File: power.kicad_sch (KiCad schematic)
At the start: 40 parts, among them J2 BATT_CON, J3 PWR_HDR, U2 BQ25622, U6 MIC2876-5.25YMT-TR

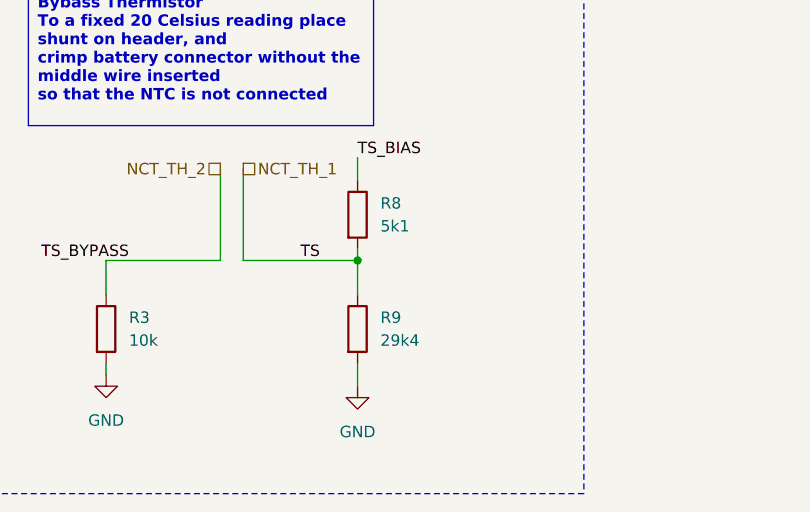
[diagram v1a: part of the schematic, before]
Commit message: fix: NTC resistor values
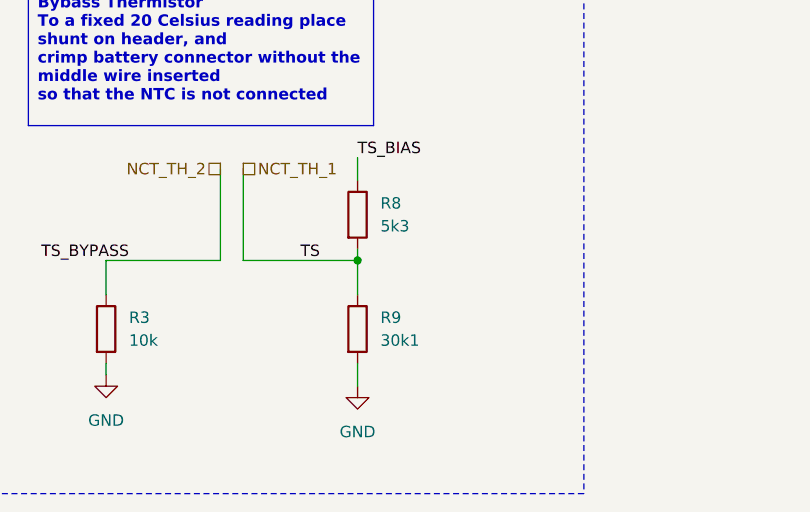
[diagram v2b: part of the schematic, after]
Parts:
- R8: value 5k1 -> 5k3; MPN ERA-2AEB512X -> RT0402DRE075K3L
- R9: value 29k4 -> 30k1; MPN ERJ-2RKF2942X -> ERA-2AEB3012X
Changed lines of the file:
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@@
 			)
 		)
-		(property "Value" "29k4"
+		(property "Value" "30k1"
 			(at 135.89 179.07 0)
 			(effects
@@
 			)
 		)
-		(property "MPN" "ERJ-2RKF2942X"
+		(property "MPN" "ERA-2AEB3012X"
 			(at 133.35 177.8 0)
 			(effects
@@
 			)
 		)
-		(property "Value" "5k1"
+		(property "Value" "5k3"
 			(at 135.89 166.37 0)
 			(effects
@@
 			)
 		)
-		(property "MPN" "ERA-2AEB512X"
+		(property "MPN" "RT0402DRE075K3L"
 			(at 133.35 165.1 0)
 			(effects

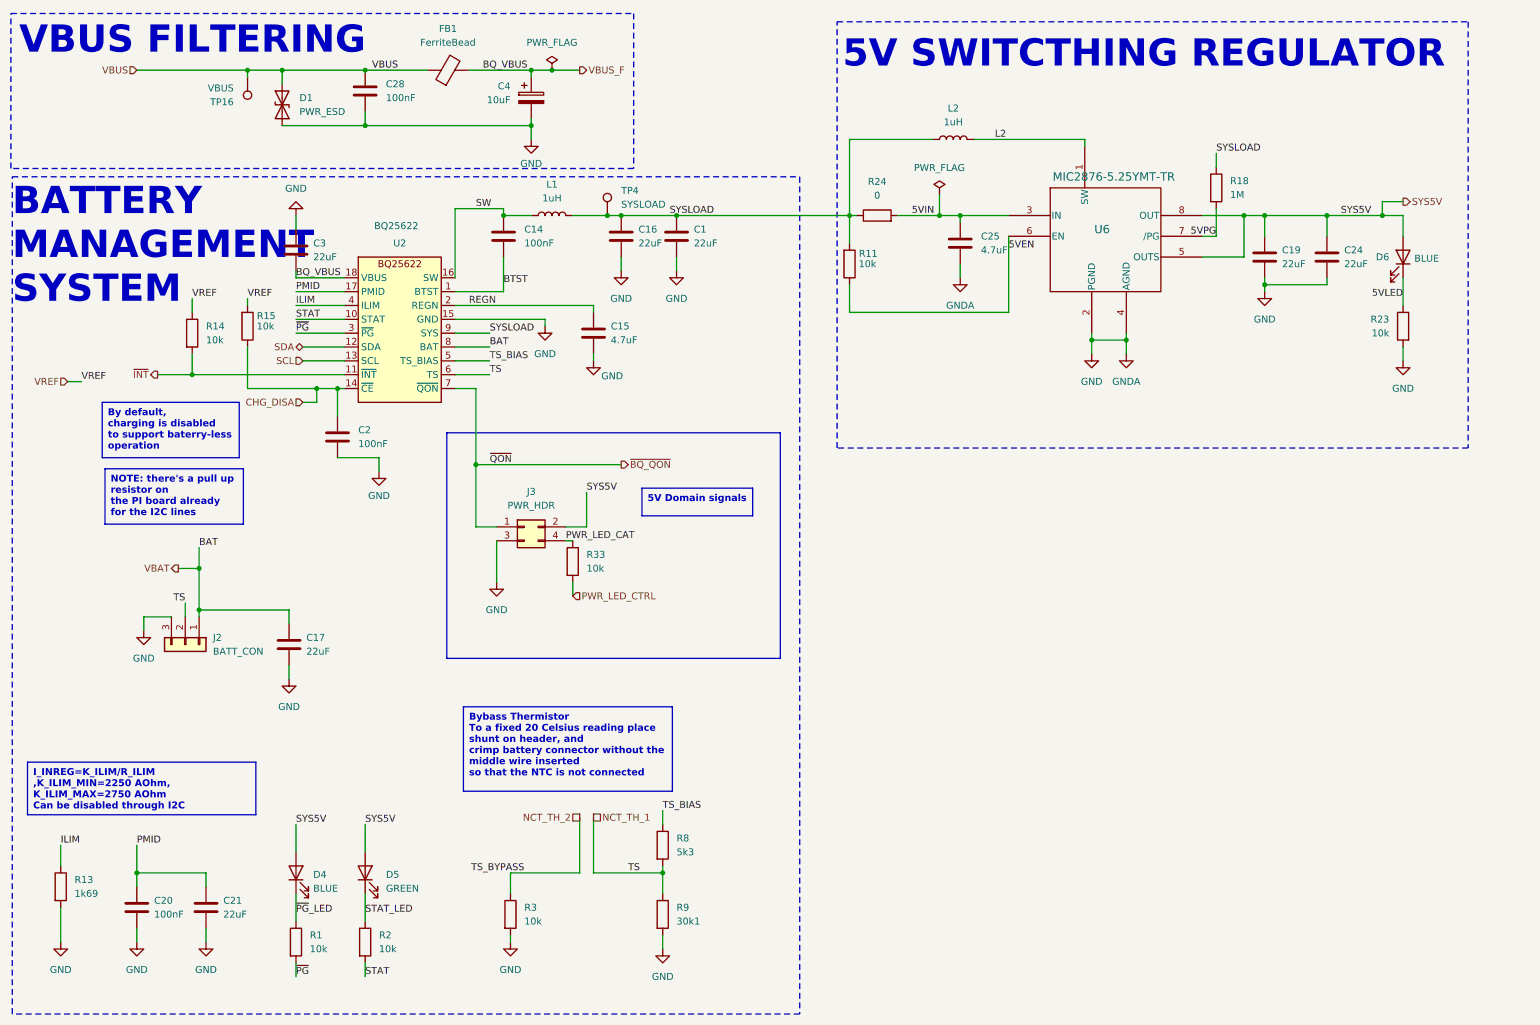
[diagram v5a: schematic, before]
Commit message: feat: 3V3 regulator + complete rework to 16 layers
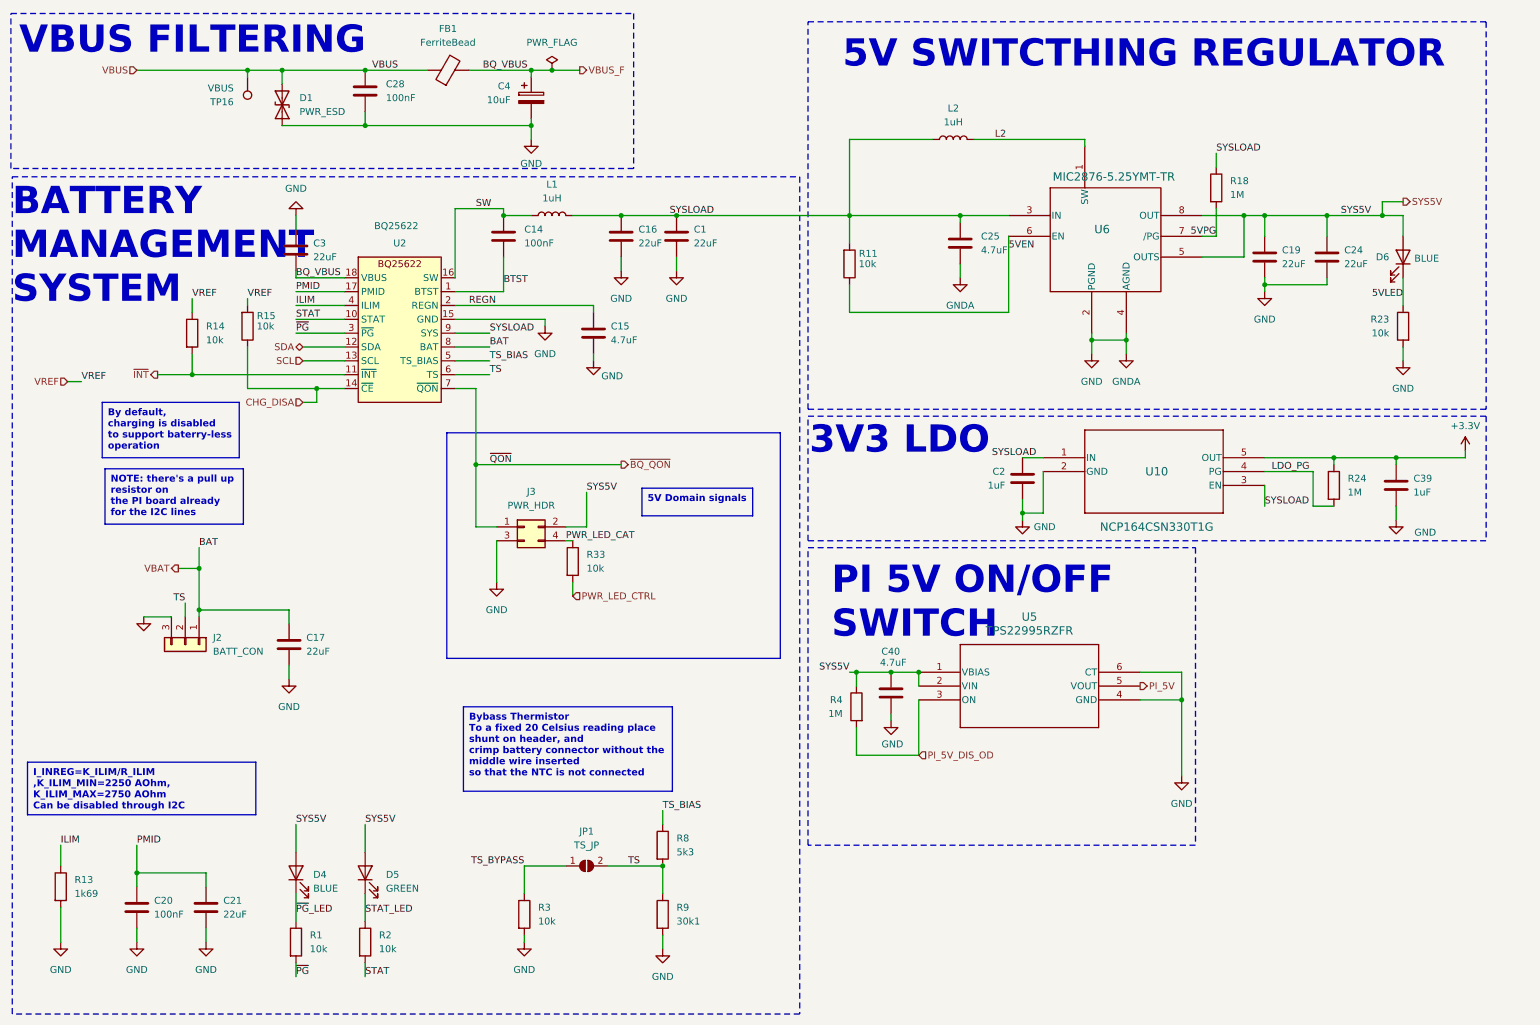
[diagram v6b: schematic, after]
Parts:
- removed TP4: SYSLOAD, TestPoint:TestPoint_Pad_D1.0mm, symbol Connector:TestPoint
- added C39: 1uF, Capacitor_SMD:C_0603_1608Metric, symbol Device:C
- added C40: 4.7uF, Capacitor_SMD:C_0603_1608Metric, symbol Device:C
- added JP1: TS_JP, Jumper:SolderJumper-2_P1.3mm_Open_TrianglePad1.0x1.5mm, symbol Jumper:SolderJumper_2_Open
- added R4: 1M, Resistor_SMD:R_0402_1005Metric, symbol Device:R
- added U10: NCP164CSN330T1G, effectiveRangeHat:FP-NCP164CSN330T1G_OSI, symbol effectiveRangeHat_kicad_sym:NCP164CSN330T1G
- added U5: TPS22995RZFR, effectiveRangeHat:WQFN6_RZF_TEX, symbol effectiveRangeHat_kicad_sym:TPS22995RZFR
- C15, C25: footprint Capacitor_SMD:C_0805_2012Metric -> Capacitor_SMD:C_0603_1608Metric; MPN GRM21BR61H475KE51L -> GRM188R6YA475KE15D; SupplierLink https://www.digikey.hu/en/products/detail/murata-electronic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 -> https://www.digikey.com/en/products/detail/murata-electroni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
- C2: value 100nF -> 1uF; footprint Capacitor_SMD:C_0402_1005Metric -> Capacitor_SMD:C_0603_1608Metric; MPN GRM155R71E104KE14J -> GCM188R71C105KA64D; SupplierLink https://www.digikey.hu/en/products/detail/murata-electronic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 -> https://www.digikey.com/en/products/detail/murata-electroni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
- R24: value 0 -> 1M; footprint Resistor_SMD:R_0603_1608Metric -> Resistor_SMD:R_0402_1005Metric; MPN ERJ-3GEY0R00V -> ERJ-2RKF1004X; SupplierLink https://www.digikey.hu/en/products/detail/panasonic-electronic-components/ERJ-3GEY0R00V/135656 -> https://www.digikey.hu/en/products/detail/panasonic-electronic-components/ERJ-2RKF1004X/79728
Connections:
- net CHG_DISA: no longer C2.1
- net GND: now also C39.2, C40.2, U10.2 (GND), U5.4 (GND), U5.6 (CT)
- net SYS5V: now also C40.1, R4.1, U5.1 (VBIAS), U5.2 (VIN)
- net SYSLOAD: now also C2.1, C25.1, U6.3 (IN), U10.1 (IN), U10.3 (EN); no longer R24.1
- removed net 5VIN: C25.1, R24.2, U6.3 (IN)
- net NCT_TH_1 renamed TS
- net TS: now also JP1.2 (B)
- net NCT_TH_2 renamed TS_BYPASS
- net TS_BYPASS: now also JP1.1 (A)
- new net +3.3V: C39.1, R24.1, U10.5 (OUT)
- new net LDO_PG: R24.2, U10.4 (PG)
- new net PI_5V: U5.5 (VOUT)
- new net PI_5V_DIS_OD: R4.2, U5.3 (ON)
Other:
- note added: "3V3 LDO"
- note added: "PI 5V ON/OFF SWITCH"
- moved on the sheet: R3
